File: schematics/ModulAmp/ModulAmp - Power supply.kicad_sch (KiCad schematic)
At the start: 10 parts, among them U2 L7805, U3 L7805, U4 MAX1044

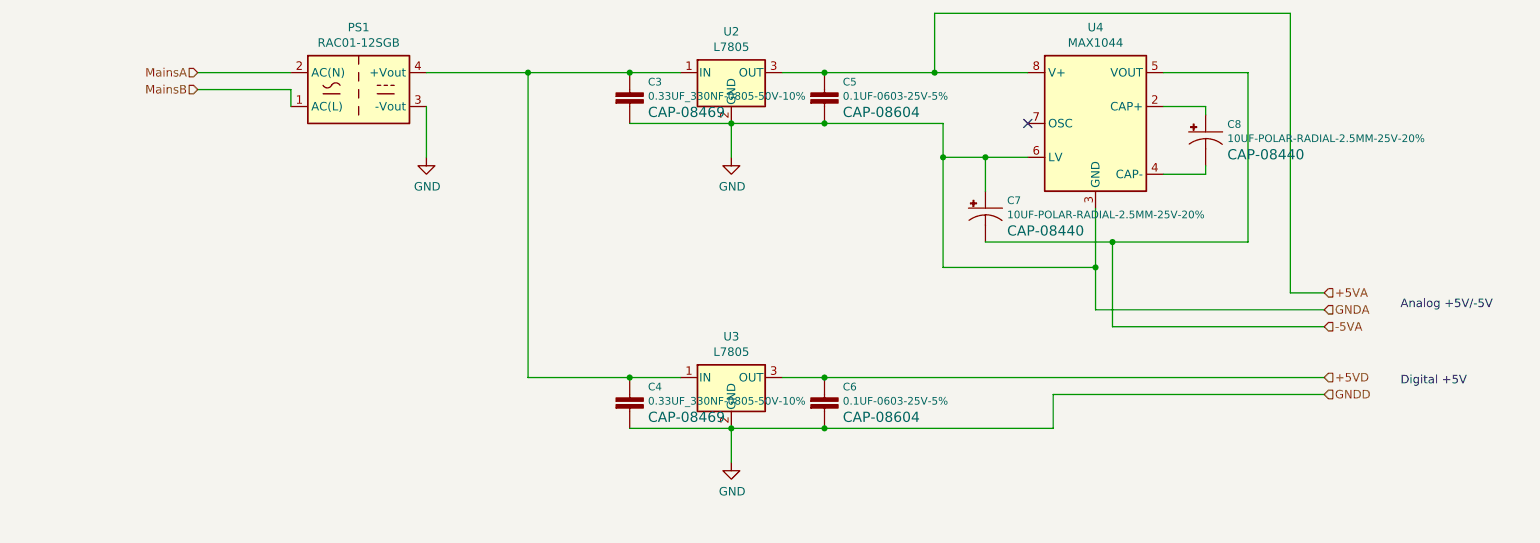
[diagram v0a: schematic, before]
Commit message: Refactored strings and added DHTxx full support
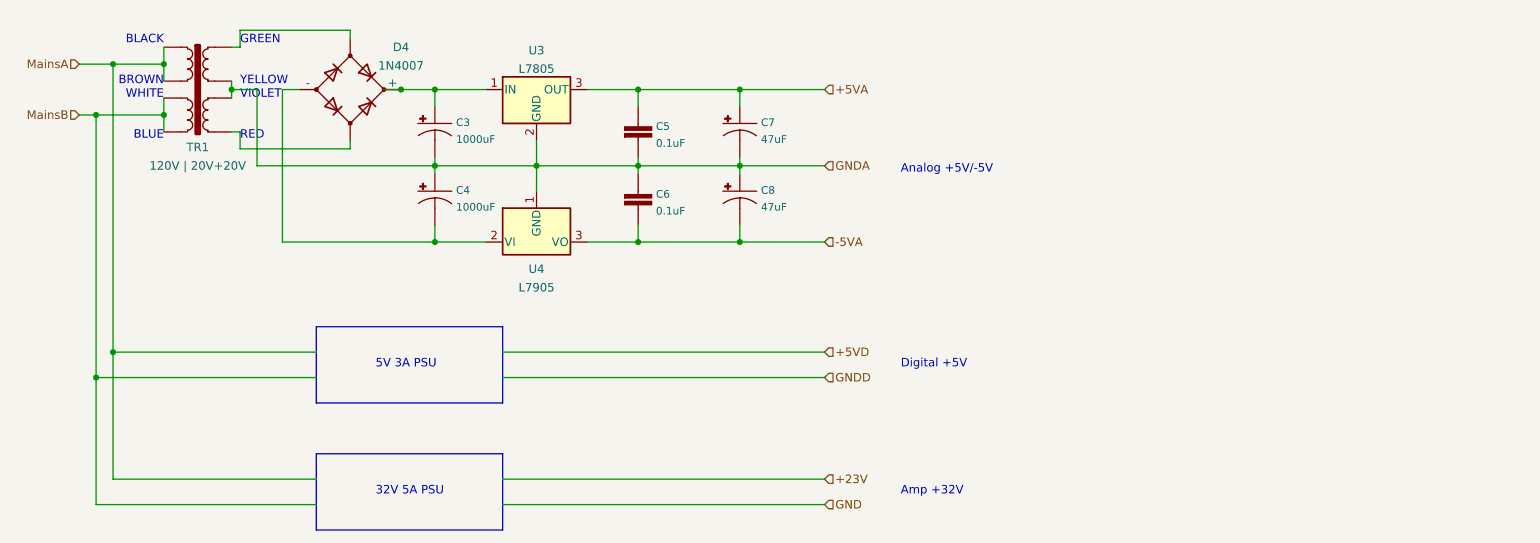
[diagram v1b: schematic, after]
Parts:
- removed C3, C4: 0.33UF_330NF-0805-50V-10%, 0805, symbol SparkFun-Capacitors:0.33UF_330NF-0805-50V-10%
- removed C7, C8: 10UF-POLAR-RADIAL-2.5MM-25V-20%, CPOL-RADIAL-2.5MM-5MM, symbol SparkFun-Capacitors:10UF-POLAR-RADIAL-2.5MM-25V-20%
- removed PS1: RAC01-12SGB, Converter_ACDC:Converter_ACDC_RECOM_RAC01-xxSGB_THT, symbol Converter_ACDC:RAC01-12SGB
- removed U2: L7805, symbol Regulator_Linear:L7805
- removed U4: MAX1044, symbol Regulator_SwitchedCapacitor:MAX1044
- added C3, C4: 1000uF, CPOL-RADIAL-5MM-10MM-KIT, symbol SparkFun-Capacitors:1000UF-RADIAL-5MM-35V-20%-KIT
- added C7, C8: 47uF, PANASONIC_D, symbol SparkFun-Capacitors:47UF-POLAR-PANASONIC_D-35V-20%
- added D4: 1N4007, symbol Device:D_Bridge_+-AA
- added TR1: 120V | 20V+20V, symbol Transformer:TRANSF6
- added U4: L7905, symbol Regulator_Linear:L7905
- C5, C6: value 0.1UF-0603-25V-5% -> 0.1uF
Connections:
- net +5VA: now also U3.3 (OUT), C7.+
- net +5VD: no longer C6.1, U3.3 (OUT)
- net -5VA: now also C6.2, C8.-, U4.3 (VO)
- net GND: no longer C5.2, C6.2, U3.2 (GND)
- net MainsA: now also TR1.1, TR1.2
- net MainsB: now also TR1.3, TR1.4
- net at U3.1 (IN): now also C3.+, D4.1 (+)
- new net: C4.-, D4.2 (-), U4.2 (VI)
- new net: D4.4, TR1.5
- new net: D4.3, TR1.8
- new net GNDA: C3.-, C4.+, C5.2, C6.1, C7.-, C8.+, TR1.6, TR1.7, U3.2 (GND), U4.1 (GND)
- no-connect marks 1 -> 0
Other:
- note added: "32V 5A PSU"
- note added: "5V 3A PSU"
- note added: "Amp +32V"
- note added: "BLACK BROWN WHITE BLUE"
- note added: "GREEN YELLOW VIOLET RED"
